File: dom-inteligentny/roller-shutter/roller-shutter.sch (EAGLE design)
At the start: 31 parts, among them K1 RP421110, K4 RP421110, Q1 16MHz, T1 BC847, T2 BC847, U1 ATMEGA328, X2 JST-XH-05-PIN-LONG-PAD, X3 JST-XH-05-PIN-LONG-PAD

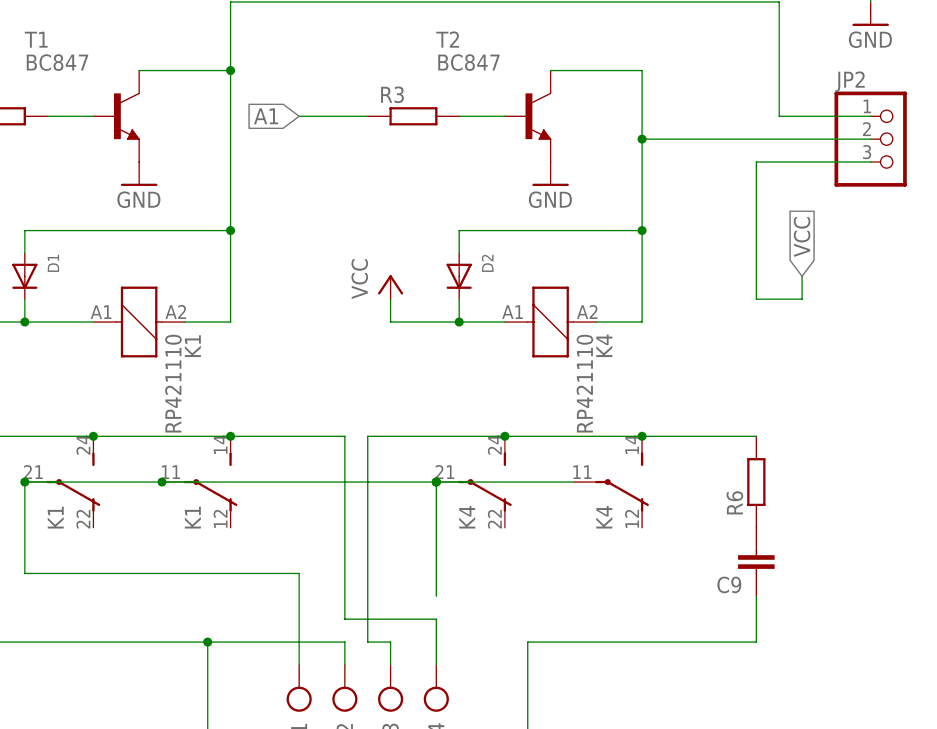
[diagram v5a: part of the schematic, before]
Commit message: adds SSR to roller shutter controller
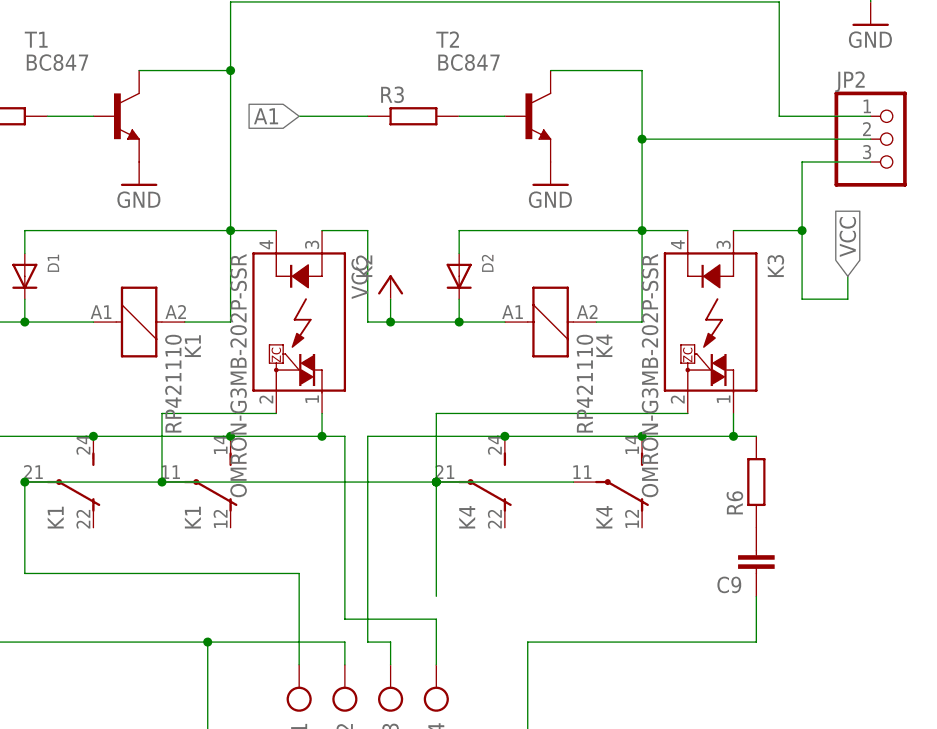
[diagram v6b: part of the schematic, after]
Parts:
- added K2, K3: OMRON-G3MB-202P-SSR, Omron G3MB 202p SSR:OMRON-G3MB-202P-SSR
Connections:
- net N$1: now also K2.K
- net N$2: now also K3.K
- net N$4: now also K2.DS2, K3.DS2
- net N$7: now also K2.DS1
- net N$8: now also K3.DS1
- net VCC: now also K2.A, K3.A
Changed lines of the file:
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@@
 <layer number="112" name="tSilk" color="7" fill="1" visible="yes" active="yes"/>
 <layer number="113" name="IDFDebug" color="4" fill="1" visible="yes" active="yes"/>
+<layer number="114" name="Badge_Outline" color="7" fill="1" visible="yes" active="yes"/>
+<layer number="115" name="ReferenceISLANDS" color="7" fill="1" visible="yes" active="yes"/>
 <layer number="116" name="Patch_BOT" color="9" fill="4" visible="no" active="yes"/>
 <layer number="118" name="Rect_Pads" color="7" fill="1" visible="no" active="no"/>
@@
 <part name="JP6" library="pinhead-zmiany-JP" deviceset="PINHD-3X4" device=""/>
 <part name="X5" library="con-ptr500" library_urn="urn:adsk.eagle:library:181" deviceset="AK500/4" device="" package3d_urn="urn:adsk.eagle:package:9887/1"/>
+<part name="K2" library="Omron G3MB 202p SSR" deviceset="OMRON-G3MB-202P-SSR" device=""/>
+<part name="K3" library="Omron G3MB 202p SSR" deviceset="OMRON-G3MB-202P-SSR" device=""/>
 </parts>
 <sheets>
@@
 <attribute name="NAME" x="308.991" y="41.91" size="1.778" layer="95" rot="R270"/>
 <attribute name="VALUE" x="313.563" y="39.37" size="1.778" layer="96" rot="R90"/>
+</instance>
+<instance part="K2" gate="G$1" x="294.64" y="86.36" smashed="yes" rot="R270">
+<attribute name="NAME" x="300.99" y="93.98" size="1.778" layer="95" font="vector" rot="R270"/>
+<attribute name="VALUE" x="287.02" y="93.98" size="1.778" layer="96" font="vector" rot="R270"/>
+</instance>
+<instance part="K3" gate="G$1" x="340.36" y="86.36" smashed="yes" rot="R270">
+<attribute name="NAME" x="346.71" y="93.98" size="1.778" layer="95" font="vector" rot="R270"/>
+<attribute name="VALUE" x="332.74" y="93.98" size="1.778" layer="96" font="vector" rot="R270"/>
 </instance>
 </instances>
@@
 <wire x1="312.42" y1="88.9" x2="312.42" y2="86.36" width="0.1524" layer="91"/>
 <junction x="312.42" y="86.36"/>
+<pinref part="K2" gate="G$1" pin="A"/>
+<wire x1="297.18" y1="96.52" x2="302.26" y2="96.52" width="0.1524" layer="91"/>
+<wire x1="302.26" y1="96.52" x2="302.26" y2="86.36" width="0.1524" layer="91"/>
+<wire x1="302.26" y1="86.36" x2="304.8" y2="86.36" width="0.1524" layer="91"/>
+<junction x="304.8" y="86.36"/>
 </segment>
 <segment>
@@
 <segment>
 <pinref part="JP2" gate="A" pin="3"/>
-<wire x1="358.14" y1="104.14" x2="345.44" y2="104.14" width="0.1524" layer="91"/>
-<wire x1="345.44" y1="104.14" x2="345.44" y2="88.9" width="0.1524" layer="91"/>
-<wire x1="345.44" y1="88.9" x2="350.52" y2="88.9" width="0.1524" layer="91"/>
-<wire x1="350.52" y1="88.9" x2="350.52" y2="91.44" width="0.1524" layer="91"/>
-<label x="350.52" y="91.44" size="1.778" layer="95" rot="R90" xref="yes"/>
+<wire x1="358.14" y1="104.14" x2="350.52" y2="104.14" width="0.1524" layer="91"/>
+<wire x1="350.52" y1="104.14" x2="350.52" y2="96.52" width="0.1524" layer="91"/>
+<wire x1="350.52" y1="96.52" x2="350.52" y2="88.9" width="0.1524" layer="91"/>
+<wire x1="350.52" y1="88.9" x2="355.6" y2="88.9" width="0.1524" layer="91"/>
+<wire x1="355.6" y1="88.9" x2="355.6" y2="91.44" width="0.1524" layer="91"/>
+<label x="355.6" y="91.44" size="1.778" layer="95" rot="R90" xref="yes"/>
+<pinref part="K3" gate="G$1" pin="A"/>
+<wire x1="342.9" y1="96.52" x2="350.52" y2="96.52" width="0.1524" layer="91"/>
+<junction x="350.52" y="96.52"/>
 </segment>
 <segment>
@@
 <pinref part="JP2" gate="A" pin="1"/>
 <wire x1="347.98" y1="109.22" x2="358.14" y2="109.22" width="0.1524" layer="91"/>
+<pinref part="K2" gate="G$1" pin="K"/>
+<wire x1="292.1" y1="96.52" x2="287.02" y2="96.52" width="0.1524" layer="91"/>
 </segment>
 </net>
@@
 <wire x1="358.14" y1="106.68" x2="332.74" y2="106.68" width="0.1524" layer="91"/>
 <junction x="332.74" y="106.68"/>
+<pinref part="K3" gate="G$1" pin="K"/>
+<wire x1="337.82" y1="96.52" x2="332.74" y2="96.52" width="0.1524" layer="91"/>
 </segment>
 </net>
@@
 <wire x1="294.64" y1="48.26" x2="294.64" y2="58.42" width="0.1524" layer="91"/>
 <pinref part="X5" gate="-1" pin="KL"/>
+<pinref part="K3" gate="G$1" pin="DS2"/>
+<wire x1="337.82" y1="76.2" x2="309.88" y2="76.2" width="0.1524" layer="91"/>
+<wire x1="309.88" y1="76.2" x2="309.88" y2="68.58" width="0.1524" layer="91"/>
+<pinref part="K2" gate="G$1" pin="DS2"/>
+<wire x1="292.1" y1="76.2" x2="279.4" y2="76.2" width="0.1524" layer="91"/>
+<wire x1="279.4" y1="76.2" x2="279.4" y2="68.58" width="0.1524" layer="91"/>
 </segment>
 </net>
@@
 <pinref part="K1" gate="2" pin="S"/>
 <wire x1="271.78" y1="73.66" x2="287.02" y2="73.66" width="0.1524" layer="91"/>
-<wire x1="287.02" y1="73.66" x2="299.72" y2="73.66" width="0.1524" layer="91"/>
+<wire x1="287.02" y1="73.66" x2="297.18" y2="73.66" width="0.1524" layer="91"/>
 <junction x="287.02" y="73.66"/>
+<wire x1="297.18" y1="73.66" x2="299.72" y2="73.66" width="0.1524" layer="91"/>
 <wire x1="299.72" y1="73.66" x2="299.72" y2="53.34" width="0.1524" layer="91"/>
 <wire x1="299.72" y1="53.34" x2="309.88" y2="53.34" width="0.1524" layer="91"/>
@@
 <wire x1="271.78" y1="73.66" x2="251.46" y2="73.66" width="0.1524" layer="91"/>
 <junction x="271.78" y="73.66"/>
+<pinref part="K2" gate="G$1" pin="DS1"/>
+<wire x1="297.18" y1="76.2" x2="297.18" y2="73.66" width="0.1524" layer="91"/>
+<junction x="297.18" y="73.66"/>
 </segment>
 </net>
@@
 <wire x1="304.8" y1="50.8" x2="304.8" y2="48.26" width="0.1524" layer="91"/>
 <pinref part="R6" gate="G$1" pin="2"/>
-<wire x1="345.44" y1="73.66" x2="332.74" y2="73.66" width="0.1524" layer="91"/>
+<wire x1="345.44" y1="73.66" x2="342.9" y2="73.66" width="0.1524" layer="91"/>
 <junction x="332.74" y="73.66"/>
-</segment>
-</net>
+<pinref part="K3" gate="G$1" pin="DS1"/>
+<wire x1="342.9" y1="73.66" x2="332.74" y2="73.66" width="0.1524" layer="91"/>
+<wire x1="342.9" y1="76.2" x2="342.9" y2="73.66" width="0.1524" layer="91"/>
+<junction x="342.9" y="73.66"/>
+</segment>
+</net>
